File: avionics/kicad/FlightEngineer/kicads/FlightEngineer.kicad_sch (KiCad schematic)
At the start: 151 parts

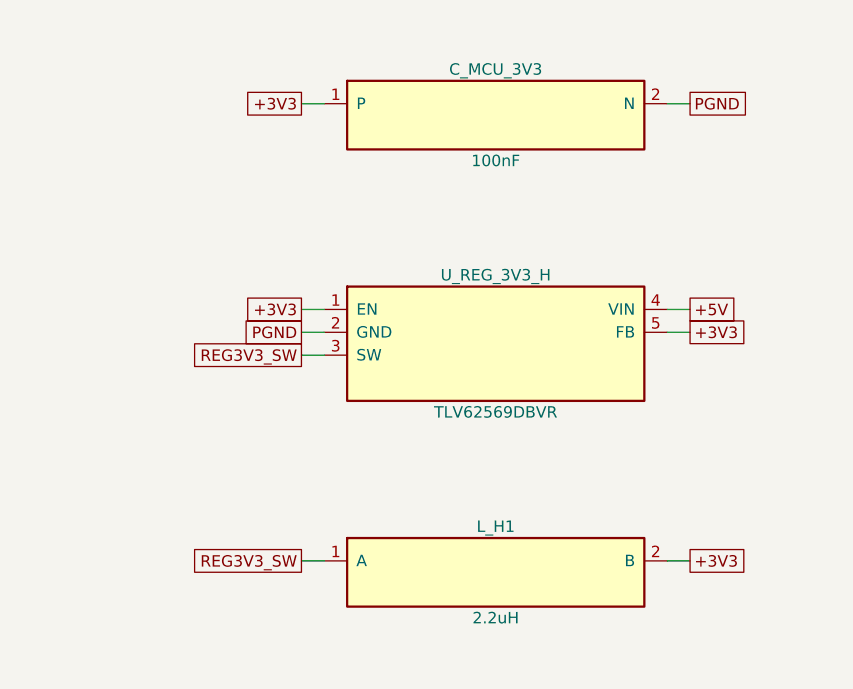
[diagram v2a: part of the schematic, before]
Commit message: fix(avionics): TLV62569 -> TLV62569PDRLR and TLV75725 -> TLV75725PDRVR package swaps; regulator circuit fixes; stale-component cleanup
Owner-approved swaps (2026-09-26, avionics/WBS.md U7.1e) using the
datasheet-verified SecureControllers library via ${SECURE_CONTROLLERS_LIB}:
- CAN-PERIPH-GW-1 U_REG_3V3, Observer U_REG_3V3/U_REG_1V2, Flight
  Engineer U_REG_3V3_H -> TLV62569PDRLR (SOT-563, 1.6 x 1.6 mm).
  Pins remapped by name; the old symbols had FB/PG swapped (gateway,
  Observer) or sat on a 3-pad SOT-23 (Flight Engineer).
- Observer U_REG_2V5 -> TLV75725PDRVR (WSON-6 2x2, EP to GND).
- Feedback dividers per TLV62569 Sec. 8.2.2.2 Eq. 2 (VFB 0.6 V):
  gateway 10k/20k (0.9 V!) -> 453k/100k = 3.318 V; Observer placeholders
  -> 453k/100k (3V3) and 100k/100k (1V2).
- Flight Engineer: EN was tied to its own 3V3 output and FB straight to
  +3V3 (would regulate at 0.6 V); EN -> +5V, added R_H_FBT 453k /
  R_H_FBB 100k. Parity 2 -> 0, ERC 0.
- tools/kicad_prune_stale.py: parity-driven removal of stale electrical
  footprints and only the copper they orphan; mounting holes are marked
  board_only + renumbered (Commo parity 93 -> 86, Observer 21 -> 17).
- New tools kicad_relink.py / kicad_add_part.py / kicad_set_value.py;
  SecureControllers entries added to every board's lib tables.

Sources: TI TLV62569 (SLVSDG1C) Pin Functions, Sec. 8.2.2.2; TI TLV757P
Fig. 4-3, Pin Functions, DRV0006A.

AI-authored: Claude Opus 5.5 (Anthropic).

Co-Authored-By: Claude Opus 5.5 <noreply@anthropic.com>
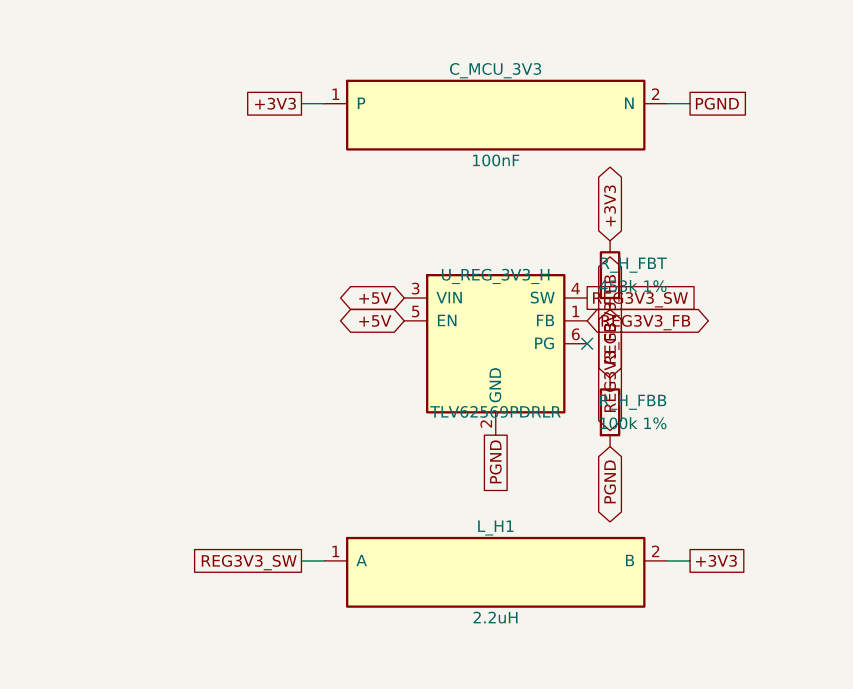
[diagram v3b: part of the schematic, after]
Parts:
- added R_H_FBB: 100k 1%, Resistor_SMD:R_0402_1005Metric, symbol Device:R
- added R_H_FBT: 453k 1%, Resistor_SMD:R_0402_1005Metric, symbol Device:R
- U_REG_3V3_H: value TLV62569DBVR -> TLV62569PDRLR; footprint Package_TO_SOT_SMD:SOT-23 -> Package_TO_SOT_SMD:SOT-563; symbol FlightEngineer:S_U_REG_3V3_H -> SecureControllers:TLV62569PDRL
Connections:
- net +3V3: now also R_H_FBT.1; no longer U_REG_3V3_H.1 (EN), U_REG_3V3_H.5 (FB)
- net +5V: now also U_REG_3V3_H.3 (VIN), U_REG_3V3_H.5 (EN); no longer U_REG_3V3_H.4 (VIN)
- net PGND: now also R_H_FBB.2
- net REG3V3_SW: now also U_REG_3V3_H.4 (SW); no longer U_REG_3V3_H.3 (SW)
- new net REG3V3_FB: R_H_FBB.1, R_H_FBT.2, U_REG_3V3_H.1 (FB)
- no-connect marks 32 -> 33
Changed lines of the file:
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@@
   (wire (pts (xy 857.25 238.76) (xy 859.79 238.76)) (stroke (width 0) (type default)))
   (global_label "PGND" (shape passive) (at 859.79 238.76 0) (effects (font (size 1.27 1.27)) (justify left)))
-  (symbol (lib_id "FlightEngineer:S_U_REG_3V3_H") (at 838.20 265.43 0) (unit 1)
+  (symbol (lib_id "SecureControllers:TLV62569PDRL") (at 838.20 265.43 0) (unit 1)
     (exclude_from_sim no) (in_bom yes) (on_board yes) (dnp no)
     (property "Reference" "U_REG_3V3_H" (at 838.20 257.81 0) (effects (font (size 1.27 1.27))))
-    (property "Value" "TLV62569DBVR" (at 838.20 273.05 0) (effects (font (size 1.27 1.27))))
-    (property "Footprint" "Package_TO_SOT_SMD:SOT-23" (at 838.20 265.43 0) (effects (font (size 1.27 1.27)) (hide yes)))
-    (property "Datasheet" "5V->3V3 buck for the trust-module logic domain" (at 838.20 265.43 0) (effects (font (size 1.27 1.27)) (hide yes)))
+    (property "Value" "TLV62569PDRLR" (at 838.20 273.05 0) (effects (font (size 1.27 1.27))))
+    (property "Footprint" "Package_TO_SOT_SMD:SOT-563" (at 838.20 265.43 0) (effects (font (size 1.27 1.27)) (hide yes)))
+    (property "Datasheet" "https://www.ti.com/lit/ds/symlink/tlv62569.pdf" (at 838.20 265.43 0) (effects (font (size 1.27 1.27)) (hide yes)))
     (property "MPN" "TLV62569DBVR" (at 838.20 265.43 0) (effects (font (size 1.27 1.27)) (hide yes)))
     (pin "1")
@@
     (instances (project "FlightEngineer" (path "/fe000000-0000-0000-0000-000000000001" (reference "U_REG_3V3_H") (unit 1))))
   )
-  (wire (pts (xy 819.15 261.62) (xy 816.61 261.62)) (stroke (width 0) (type default)))
-  (global_label "+3V3" (shape passive) (at 816.61 261.62 180) (effects (font (size 1.27 1.27)) (justify right)))
-  (wire (pts (xy 819.15 264.16) (xy 816.61 264.16)) (stroke (width 0) (type default)))
-  (global_label "PGND" (shape passive) (at 816.61 264.16 180) (effects (font (size 1.27 1.27)) (justify right)))
-  (wire (pts (xy 819.15 266.70) (xy 816.61 266.70)) (stroke (width 0) (type default)))
-  (global_label "REG3V3_SW" (shape passive) (at 816.61 266.70 180) (effects (font (size 1.27 1.27)) (justify right)))
-  (wire (pts (xy 857.25 261.62) (xy 859.79 261.62)) (stroke (width 0) (type default)))
-  (global_label "+5V" (shape passive) (at 859.79 261.62 0) (effects (font (size 1.27 1.27)) (justify left)))
-  (wire (pts (xy 857.25 264.16) (xy 859.79 264.16)) (stroke (width 0) (type default)))
-  (global_label "+3V3" (shape passive) (at 859.79 264.16 0) (effects (font (size 1.27 1.27)) (justify left)))
+  (global_label "PGND" (shape passive) (at 838.2000 275.5900 270) (effects (font (size 1.27 1.27))))
+  (global_label "REG3V3_SW" (shape passive) (at 848.3600 260.3500 0) (effects (font (size 1.27 1.27))))
   (symbol (lib_id "FlightEngineer:S_L_H1") (at 838.20 290.83 0) (unit 1)
     (exclude_from_sim no) (in_bom yes) (on_board yes) (dnp no)
@@
 		(effects (font (size 1.27 1.27)) (justify left top))
 	)
-	(sheet_instances (path "/" (page "1")))
-)
+	(global_label "+5V" (shape bidirectional) (at 828.0400 262.8900 180)
+    (effects (font (size 1.27 1.27)))
+)
+  (global_label "REG3V3_FB" (shape bidirectional) (at 848.3600 262.8900 0)
+    (effects (font (size 1.27 1.27)))
+)
+  (global_label "+5V" (shape bidirectional) (at 828.0400 260.3500 180)
+    (effects (font (size 1.27 1.27)))
+)
+  (no_connect (at 848.3600 265.4300))
+  (symbol (lib_id "Device:R") (at 850.90 257.81 0) (unit 1)
+    (exclude_from_sim no) (in_bom yes) (on_board yes) (dnp no)
+    (property "Reference" "R_H_FBT" (at 853.44 256.54 0) (effects (font (size 1.27 1.27))))
+    (property "Value" "453k 1%" (at 853.44 259.08 0) (effects (font (size 1.27 1.27))))
+    (property "Footprint" "Resistor_SMD:R_0402_1005Metric" (at 850.90 257.81 0) (effects (font (size 1.27 1.27)) (hide yes)))
+    (property "Datasheet" "" (at 850.90 257.81 0) (effects (font (size 1.27 1.27)) (hide yes)))
+    (pin "1")
+    (pin "2")
+    (instances (project "FlightEngineer" (path "/fe000000-0000-0000-0000-000000000001" (reference "R_H_FBT") (unit 1)))))
+  (global_label "+3V3" (shape bidirectional) (at 850.9000 254.0000 90)
+    (effects (font (size 1.27 1.27)))
+)
+  (global_label "REG3V3_FB" (shape bidirectional) (at 850.9000 261.6200 270)
+    (effects (font (size 1.27 1.27)))
+)
+  (symbol (lib_id "Device:R") (at 850.90 273.05 0) (unit 1)
+    (exclude_from_sim no) (in_bom yes) (on_board yes) (dnp no)
+    (property "Reference" "R_H_FBB" (at 853.44 271.78 0) (effects (font (size 1.27 1.27))))
+    (property "Value" "100k 1%" (at 853.44 274.32 0) (effects (font (size 1.27 1.27))))
+    (property "Footprint" "Resistor_SMD:R_0402_1005Metric" (at 850.90 273.05 0) (effects (font (size 1.27 1.27)) (hide yes)))
+    (property "Datasheet" "" (at 850.90 273.05 0) (effects (font (size 1.27 1.27)) (hide yes)))
+    (pin "1")
+    (pin "2")
+    (instances (project "FlightEngineer" (path "/fe000000-0000-0000-0000-000000000001" (reference "R_H_FBB") (unit 1)))))
+  (global_label "REG3V3_FB" (shape bidirectional) (at 850.9000 269.2400 90)
+    (effects (font (size 1.27 1.27)))
+)
+  (global_label "PGND" (shape bidirectional) (at 850.9000 276.8600 270)
+    (effects (font (size 1.27 1.27)))
+)
+  (sheet_instances (path "/" (page "1")))
+)

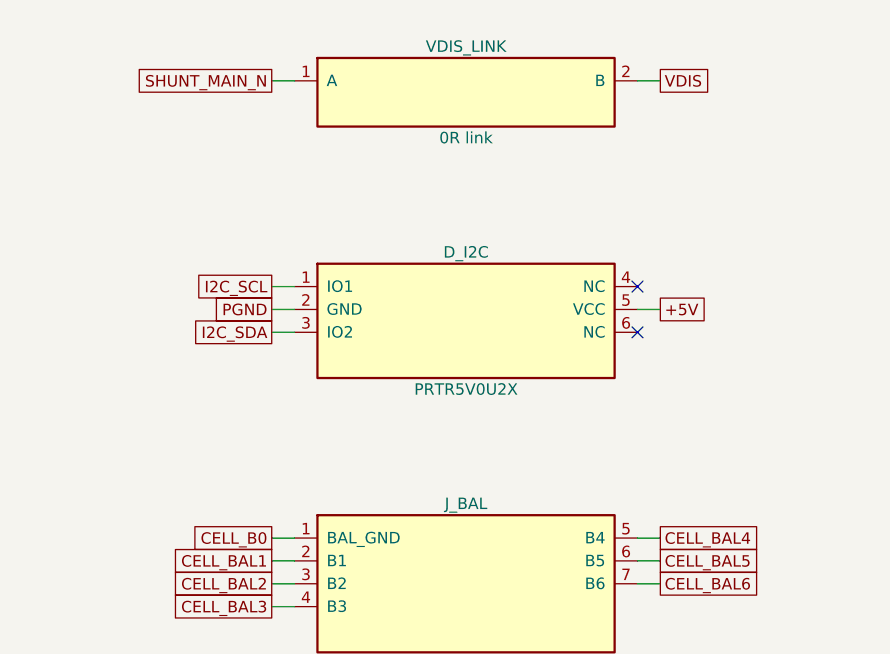
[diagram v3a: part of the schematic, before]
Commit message: fix(avionics): PRTR5V0U2X package/pinout fix on all 12 instances, 5 boards
Owner-approved 2026-09-26 (avionics/WBS.md U7.2). Per Nexperia
PRTR5V0U2X datasheet Table 2 (SOT143B: 1=GND, 2=I/O1, 3=I/O2, 4=VCC),
relinked via tools/kicad_relink.py --rewire (same footprint position/
rotation preserved, only package + pin-to-net correspondence corrected):

- Pilot TVS-CAN, TVS-RS485; TACCO TVS-CAN, TVS-RS485; FlightEngineer
  D_I2C: straightforward SOT-363->SOT-143 swap with existing GND/VCC
  nets carried over unchanged (5 instances).
- Observer T1_D1/T1_D2/T2_D1/T2_D2 (Ethernet magnetics ESD) and D5
  (CAN-FD), Commo 'ANT TVS' and 'UART TVS': these had no VCC net at
  all in the original (wrong-package) design -- VCC tied to the local
  GND/PGND net as a conservative fallback (line-to-line and
  line-to-ground clamping preserved; the rail-clamp direction is
  inert). This is a judgment call, not a datasheet requirement --
  flagged for review, not a silent assumption (7 instances).

ERC unchanged (0/0/0/0/154-pre-existing) on all 5 boards; DRC/parity
flat or improved except one new courtyard-overlap warning on Pilot
(TVS-CAN vs C-IN1, mechanical only) left unresolved rather than guess
a nudge direction without full layout context.

AI-authored: Claude Sonnet 5 (Anthropic).

Co-Authored-By: Claude Sonnet 5 <noreply@anthropic.com>
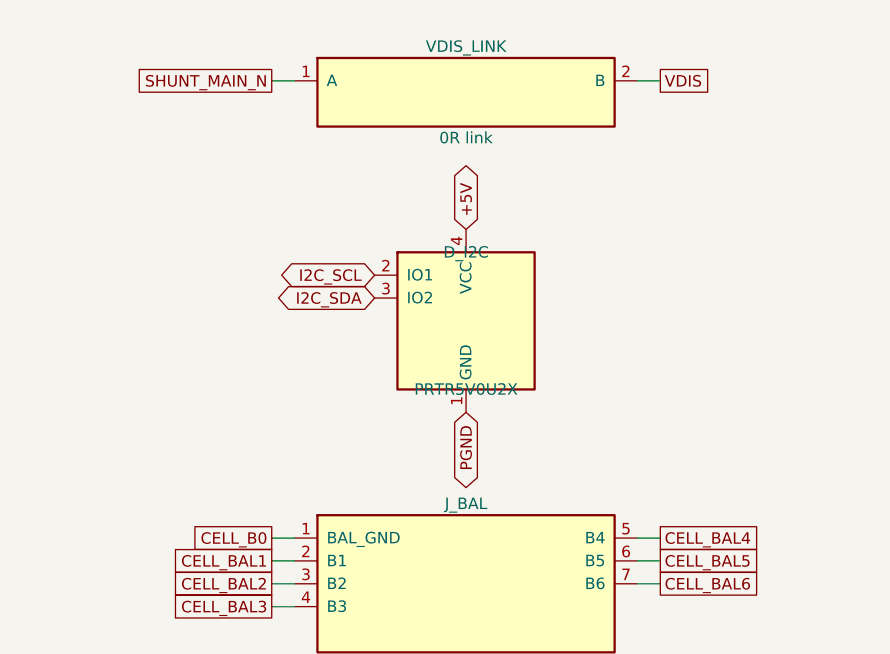
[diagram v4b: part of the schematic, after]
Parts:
- D_I2C: footprint Package_TO_SOT_SMD:SOT-363_SC-70-6 -> Package_TO_SOT_SMD:SOT-143; symbol FlightEngineer:S_D_I2C -> SecureControllers:PRTR5V0U2X
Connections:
- net +5V: now also D_I2C.4 (VCC); no longer D_I2C.5 (VCC)
- net I2C_SCL: now also D_I2C.2 (IO1); no longer D_I2C.1 (IO1)
- net PGND: now also D_I2C.1 (GND); no longer D_I2C.2 (GND)
- no-connect marks 33 -> 31
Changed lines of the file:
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@@
   (wire (pts (xy 222.25 396.24) (xy 224.79 396.24)) (stroke (width 0) (type default)))
   (global_label "VDIS" (shape passive) (at 224.79 396.24 0) (effects (font (size 1.27 1.27)) (justify left)))
-  (symbol (lib_id "FlightEngineer:S_D_I2C") (at 203.20 422.91 0) (unit 1)
+  (symbol (lib_id "SecureControllers:PRTR5V0U2X") (at 203.20 422.91 0) (unit 1)
     (exclude_from_sim no) (in_bom yes) (on_board yes) (dnp no)
     (property "Reference" "D_I2C" (at 203.20 415.29 0) (effects (font (size 1.27 1.27))))
     (property "Value" "PRTR5V0U2X" (at 203.20 430.53 0) (effects (font (size 1.27 1.27))))
-    (property "Footprint" "Package_TO_SOT_SMD:SOT-363_SC-70-6" (at 203.20 422.91 0) (effects (font (size 1.27 1.27)) (hide yes)))
-    (property "Datasheet" "prtr5v0u2x.pdf — I2C line RF transient protection at enclosure wall" (at 203.20 422.91 0) (effects (font (size 1.27 1.27)) (hide yes)))
+    (property "Footprint" "Package_TO_SOT_SMD:SOT-143" (at 203.20 422.91 0) (effects (font (size 1.27 1.27)) (hide yes)))
+    (property "Datasheet" "https://assets.nexperia.com/documents/data-sheet/PRTR5V0U2X.pdf" (at 203.20 422.91 0) (effects (font (size 1.27 1.27)) (hide yes)))
     (property "MPN" "PRTR5V0U2X,115" (at 203.20 422.91 0) (effects (font (size 1.27 1.27)) (hide yes)))
     (pin "1")
@@
     (instances (project "FlightEngineer" (path "/fe000000-0000-0000-0000-000000000001" (reference "D_I2C") (unit 1))))
   )
-  (wire (pts (xy 184.15 419.10) (xy 181.61 419.10)) (stroke (width 0) (type default)))
-  (global_label "I2C_SCL" (shape passive) (at 181.61 419.10 180) (effects (font (size 1.27 1.27)) (justify right)))
-  (wire (pts (xy 184.15 421.64) (xy 181.61 421.64)) (stroke (width 0) (type default)))
-  (global_label "PGND" (shape passive) (at 181.61 421.64 180) (effects (font (size 1.27 1.27)) (justify right)))
-  (wire (pts (xy 184.15 424.18) (xy 181.61 424.18)) (stroke (width 0) (type default)))
-  (global_label "I2C_SDA" (shape passive) (at 181.61 424.18 180) (effects (font (size 1.27 1.27)) (justify right)))
-  (no_connect (at 222.25 419.10))
-  (wire (pts (xy 222.25 421.64) (xy 224.79 421.64)) (stroke (width 0) (type default)))
-  (global_label "+5V" (shape passive) (at 224.79 421.64 0) (effects (font (size 1.27 1.27)) (justify left)))
-  (no_connect (at 222.25 424.18))
   (symbol (lib_id "FlightEngineer:S_J_BAL") (at 203.20 452.12 0) (unit 1)
     (exclude_from_sim no) (in_bom yes) (on_board yes) (dnp no)
@@
     (effects (font (size 1.27 1.27)))
 )
+  (global_label "I2C_SCL" (shape bidirectional) (at 193.0400 417.8300 180)
+    (effects (font (size 1.27 1.27)))
+)
+  (global_label "I2C_SDA" (shape bidirectional) (at 193.0400 420.3700 180)
+    (effects (font (size 1.27 1.27)))
+)
+  (global_label "PGND" (shape bidirectional) (at 203.2000 433.0700 270)
+    (effects (font (size 1.27 1.27)))
+)
+  (global_label "+5V" (shape bidirectional) (at 203.2000 412.7500 90)
+    (effects (font (size 1.27 1.27)))
+)
